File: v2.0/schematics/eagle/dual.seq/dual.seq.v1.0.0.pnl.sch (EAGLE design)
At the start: 22 parts, among them IC1 TL084P, IC2 TL084P, J1 CV3 OUT, J2 CV2 OUT, J3 CV1 OUT, J4 GATE5 OUT, J5 GATE4 OUT, J6 GATE3 OUT, J7 GATE2 OUT, J8 GATE1 OUT

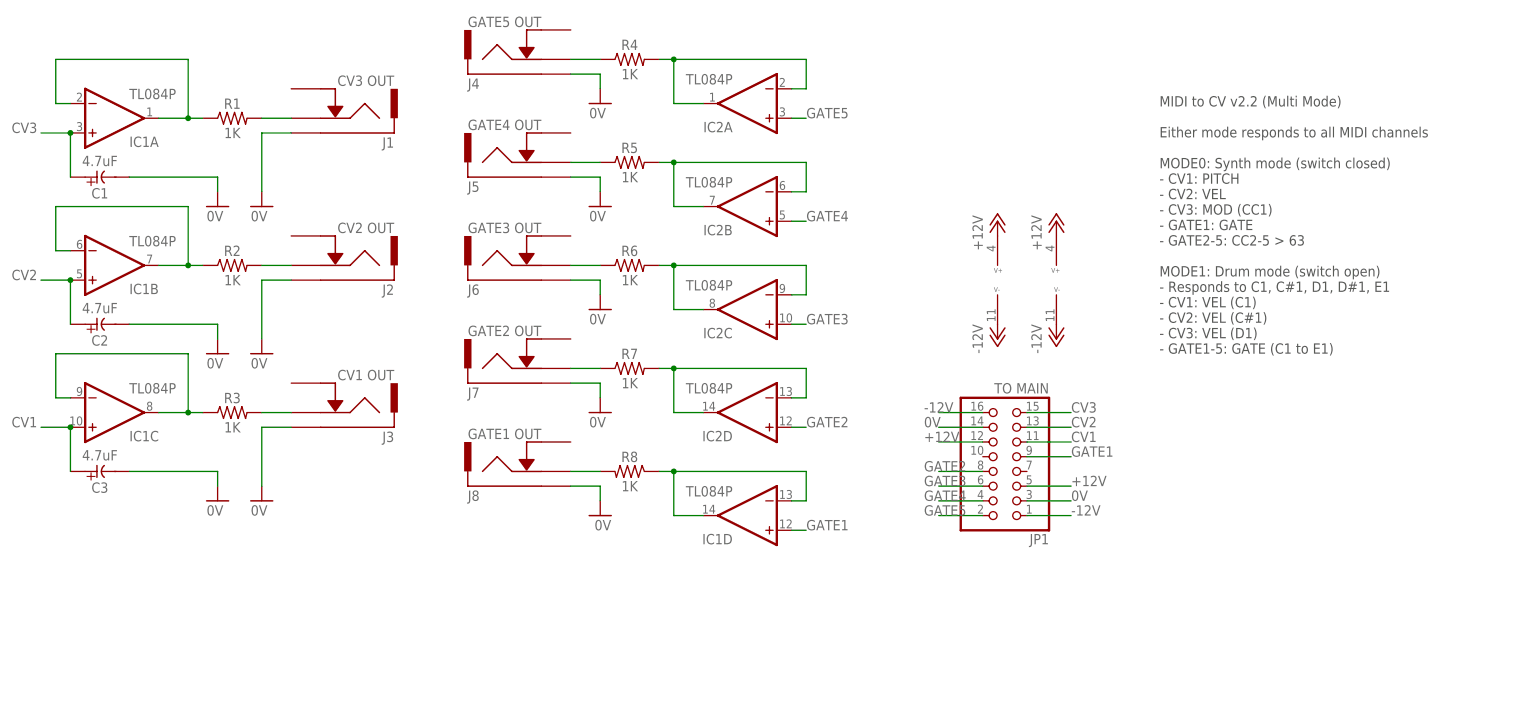
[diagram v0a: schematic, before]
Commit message: Dual seq panel schem
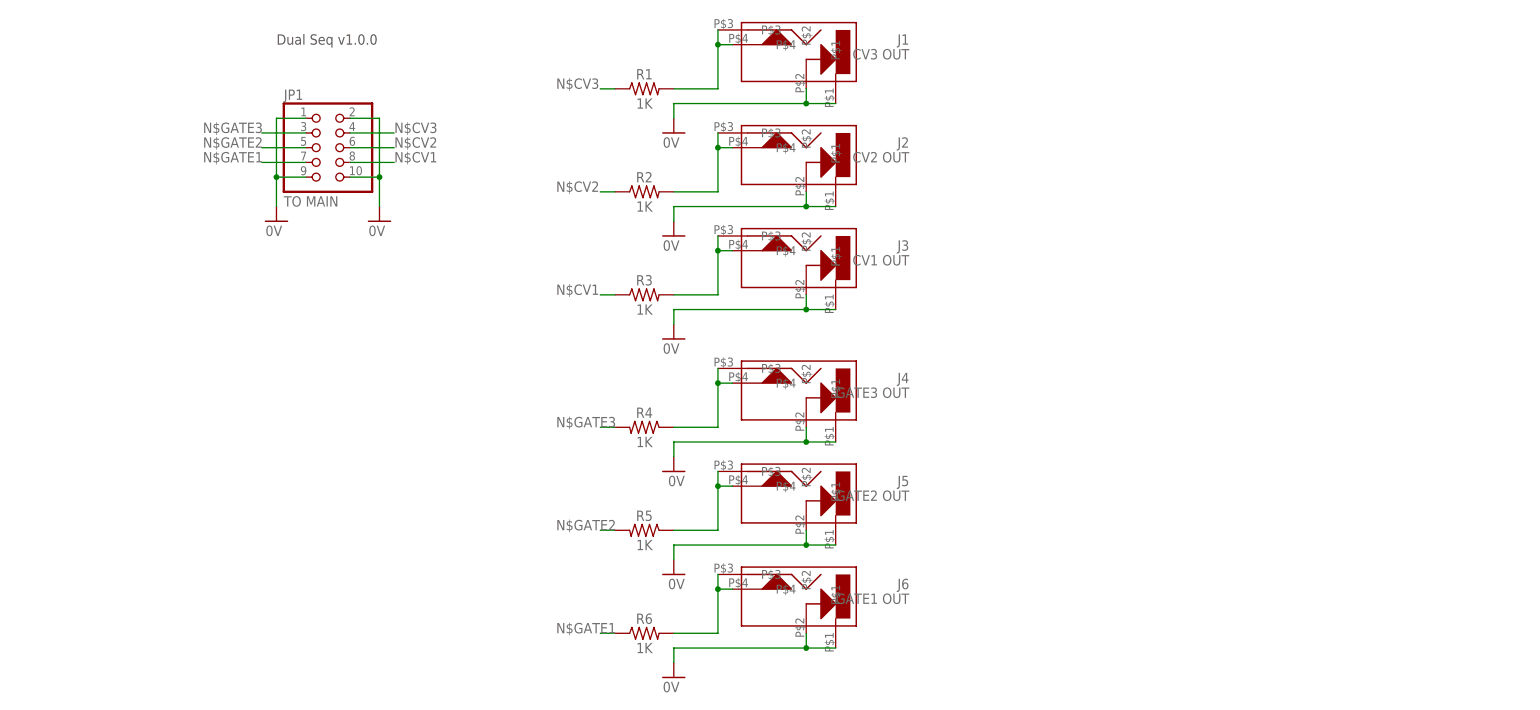
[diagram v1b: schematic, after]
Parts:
- removed C1, C2, C3: 4.7uF, _common:CE-USE2-5
- removed IC1, IC2: TL084P, _common:TL084P
- removed J7: GATE2 OUT, jacks:ACJM-MV35-2S
- removed J8: GATE1 OUT, jacks:ACJM-MV35-2S
- removed R7, R8: 1K, _common:R0309/10
- J1, J2, J3: device jacks:ACJM-MV35-2S -> jacks:CL1384
- J4: value GATE5 OUT -> GATE3 OUT; device jacks:ACJM-MV35-2S -> jacks:CL1384
- J5: value GATE4 OUT -> GATE2 OUT; device jacks:ACJM-MV35-2S -> jacks:CL1384
- J6: value GATE3 OUT -> GATE1 OUT; device jacks:ACJM-MV35-2S -> jacks:CL1384
- JP1: device pinhead:PINHD-2X8 -> pinhead:PINHD-2X5
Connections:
- removed net +12V: IC1P.V+, IC2P.V+, JP1.12, JP1.5
- removed net -12V: IC1P.V-, IC2P.V-, JP1.1, JP1.16
- removed net CV1: C3.+, IC1C.+IN, JP1.11
- removed net CV2: C2.+, IC1B.+IN, JP1.13
- removed net CV3: C1.+, IC1A.+IN, JP1.15
- removed net GATE1: IC1D.+IN, JP1.9
- removed net GATE2: IC2D.+IN, JP1.8
- removed net GATE3: IC2C.+IN, JP1.6
- removed net GATE4: IC2B.+IN, JP1.4
- removed net GATE5: IC2A.+IN, JP1.2
- removed net N$21: J4.P$2, R4.1
- removed net N$22: J5.P$2, R5.1
- removed net N$23: J6.P$2, R6.1
- removed net N$24: J7.P$2, R7.1
- removed net N$25: J8.P$2, R8.2
- removed net N$31: IC2D.-IN, IC2D.OUT, R7.2
- removed net N$35: IC2C.-IN, IC2C.OUT, R6.2
- removed net N$36: IC2B.-IN, IC2B.OUT, R5.2
- removed net N$37: IC2A.-IN, IC2A.OUT, R4.2
- removed net N$44: J1.P$2, R1.2
- removed net N$45: J2.P$2, R2.2
- removed net N$46: J3.P$2, R3.2
- removed net N$7: IC1D.-IN, IC1D.OUT, R8.1
- new net N$1: J6.P$3, J6.P$4, R6.2
- new net N$5: J2.P$3, J2.P$4, R2.2
- new net N$6: J1.P$3, J1.P$4, R1.2
- new net N$CV1: JP1.8, R3.1
- new net N$CV2: JP1.6, R2.1
- new net N$CV3: JP1.4, R1.1
- new net N$GATE1: JP1.7, R6.1
- new net N$GATE2: JP1.5, R5.2
- new net N$GATE3: JP1.3, R4.2
- net 0V: now also J1.P$2, J2.P$2, J3.P$2, J4.P$2, J5.P$2, J6.P$2, JP1.1, JP1.10, JP1.2, JP1.9; no longer C1.-, C2.-, C3.-, J7.P$1, J8.P$1, JP1.14, JP1.3
- net N$2: now also J5.P$3, J5.P$4, R5.1; no longer IC1A.-IN, IC1A.OUT, R1.1
- net N$3: now also J4.P$3, J4.P$4, R4.1; no longer IC1B.-IN, IC1B.OUT, R2.1
- net N$4: now also J3.P$3, J3.P$4, R3.2; no longer IC1C.-IN, IC1C.OUT, R3.1
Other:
- note added: "Dual Seq v1.0.0"
- note removed: "MIDI to CV v2.2 (Multi Mode) Either mode responds to all MIDI channels MODE0: Synth mode (switch closed) - CV1: PITCH - CV2: VEL - CV3: MOD (CC1) - GATE1: GATE - GATE2-5: CC2-5 > 63 MODE1: Drum mode (switch open) - Responds to C1, C#1, D1, D#1, E1 - CV1: VEL (C1) - CV2: VEL (C#1) - CV3: VEL (D1) - GATE1-5: GATE (C1 to E1)"
- moved on the sheet: R1, R2, R3, R4, R5, R6

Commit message: Added board for dual seq panel
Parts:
- R1, R2, R3, R4, R5, R6: device _common:R0309/10 -> _common:R
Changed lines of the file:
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@@
 <grid distance="0.1" unitdist="inch" unit="inch" style="lines" multiple="1" display="no" altdistance="0.01" altunitdist="inch" altunit="inch"/>
 <layers>
-<layer number="1" name="Top" color="4" fill="1" visible="no" active="no"/>
-<layer number="16" name="Bottom" color="1" fill="1" visible="no" active="no"/>
-<layer number="17" name="Pads" color="2" fill="1" visible="no" active="no"/>
-<layer number="18" name="Vias" color="2" fill="1" visible="no" active="no"/>
-<layer number="19" name="Unrouted" color="6" fill="1" visible="no" active="no"/>
-<layer number="20" name="Dimension" color="15" fill="1" visible="no" active="no"/>
-<layer number="21" name="tPlace" color="7" fill="1" visible="no" active="no"/>
-<layer number="22" name="bPlace" color="7" fill="1" visible="no" active="no"/>
-<layer number="23" name="tOrigins" color="15" fill="1" visible="no" active="no"/>
-<layer number="24" name="bOrigins" color="15" fill="1" visible="no" active="no"/>
-<layer number="25" name="tNames" color="7" fill="1" visible="no" active="no"/>
-<layer number="26" name="bNames" color="7" fill="1" visible="no" active="no"/>
-<layer number="27" name="tValues" color="7" fill="1" visible="no" active="no"/>
-<layer number="28" name="bValues" color="7" fill="1" visible="no" active="no"/>
+<layer number="1" name="Top" color="4" fill="1" visible="yes" active="no"/>
+<layer number="16" name="Bottom" color="1" fill="1" visible="yes" active="no"/>
+<layer number="17" name="Pads" color="2" fill="1" visible="yes" active="no"/>
+<layer number="18" name="Vias" color="2" fill="1" visible="yes" active="no"/>
+<layer number="19" name="Unrouted" color="6" fill="1" visible="yes" active="no"/>
+<layer number="20" name="Dimension" color="15" fill="1" visible="yes" active="no"/>
+<layer number="21" name="tPlace" color="7" fill="1" visible="yes" active="no"/>
+<layer number="22" name="bPlace" color="7" fill="1" visible="yes" active="no"/>
+<layer number="23" name="tOrigins" color="15" fill="1" visible="yes" active="no"/>
+<layer number="24" name="bOrigins" color="15" fill="1" visible="yes" active="no"/>
+<layer number="25" name="tNames" color="7" fill="1" visible="yes" active="no"/>
+<layer number="26" name="bNames" color="7" fill="1" visible="yes" active="no"/>
+<layer number="27" name="tValues" color="7" fill="1" visible="yes" active="no"/>
+<layer number="28" name="bValues" color="7" fill="1" visible="yes" active="no"/>
 <layer number="29" name="tStop" color="7" fill="3" visible="no" active="no"/>
 <layer number="30" name="bStop" color="7" fill="6" visible="no" active="no"/>
@@
 <layer number="35" name="tGlue" color="7" fill="4" visible="no" active="no"/>
 <layer number="36" name="bGlue" color="7" fill="5" visible="no" active="no"/>
-<layer number="37" name="tTest" color="7" fill="1" visible="no" active="no"/>
-<layer number="38" name="bTest" color="7" fill="1" visible="no" active="no"/>
+<layer number="37" name="tTest" color="7" fill="1" visible="yes" active="no"/>
+<layer number="38" name="bTest" color="7" fill="1" visible="yes" active="no"/>
 <layer number="39" name="tKeepout" color="4" fill="11" visible="no" active="no"/>
 <layer number="40" name="bKeepout" color="1" fill="11" visible="no" active="no"/>
@@
 <layer number="44" name="Drills" color="7" fill="1" visible="no" active="no"/>
 <layer number="45" name="Holes" color="7" fill="1" visible="no" active="no"/>
-<layer number="46" name="Milling" color="3" fill="1" visible="no" active="no"/>
-<layer number="47" name="Measures" color="7" fill="1" visible="no" active="no"/>
-<layer number="48" name="Document" color="7" fill="1" visible="no" active="no"/>
-<layer number="49" name="Reference" color="7" fill="1" visible="no" active="no"/>
-<layer number="50" name="dxf" color="7" fill="1" visible="no" active="no"/>
-<layer number="51" name="tDocu" color="7" fill="1" visible="no" active="no"/>
-<layer number="52" name="bDocu" color="7" fill="1" visible="no" active="no"/>
+<layer number="46" name="Milling" color="3" fill="1" visible="yes" active="no"/>
+<layer number="47" name="Measures" color="7" fill="1" visible="yes" active="no"/>
+<layer number="48" name="Document" color="7" fill="1" visible="yes" active="no"/>
+<layer number="49" name="Reference" color="7" fill="1" visible="yes" active="no"/>
+<layer number="50" name="dxf" color="7" fill="1" visible="yes" active="no"/>
+<layer number="51" name="tDocu" color="7" fill="1" visible="yes" active="no"/>
+<layer number="52" name="bDocu" color="7" fill="1" visible="yes" active="no"/>
 <layer number="90" name="Modules" color="5" fill="1" visible="yes" active="yes"/>
 <layer number="91" name="Nets" color="2" fill="1" visible="yes" active="yes"/>
@@
 <layer number="97" name="Info" color="7" fill="1" visible="yes" active="yes"/>
 <layer number="98" name="Guide" color="6" fill="1" visible="yes" active="yes"/>
+<layer number="99" name="SpiceOrder" color="5" fill="1" visible="yes" active="yes"/>
 <layer number="100" name="Caption" color="15" fill="0" visible="yes" active="yes"/>
 <layer number="101" name="Patch_Top" color="7" fill="1" visible="yes" active="yes"/>
@@
 <part name="GND6" library="supply1" deviceset="0V" device=""/>
 <part name="GND7" library="supply1" deviceset="0V" device=""/>
-<part name="R1" library="_common" deviceset="R" device="0309/10" value="1K"/>
-<part name="R2" library="_common" deviceset="R" device="0309/10" value="1K"/>
-<part name="R3" library="_common" deviceset="R" device="0309/10" value="1K"/>
-<part name="R6" library="_common" deviceset="R" device="0309/10" value="1K"/>
-<part name="R4" library="_common" deviceset="R" device="0309/10" value="1K"/>
-<part name="R5" library="_common" deviceset="R" device="0309/10" value="1K"/>
+<part name="R1" library="_common" deviceset="R" device="" value="1K"/>
+<part name="R2" library="_common" deviceset="R" device="" value="1K"/>
+<part name="R3" library="_common" deviceset="R" device="" value="1K"/>
+<part name="R6" library="_common" deviceset="R" device="" value="1K"/>
+<part name="R4" library="_common" deviceset="R" device="" value="1K"/>
+<part name="R5" library="_common" deviceset="R" device="" value="1K"/>
 <part name="J4" library="jacks" deviceset="CL1384" device="" value="GATE3 OUT"/>
 <part name="J5" library="jacks" deviceset="CL1384" device="" value="GATE2 OUT"/>

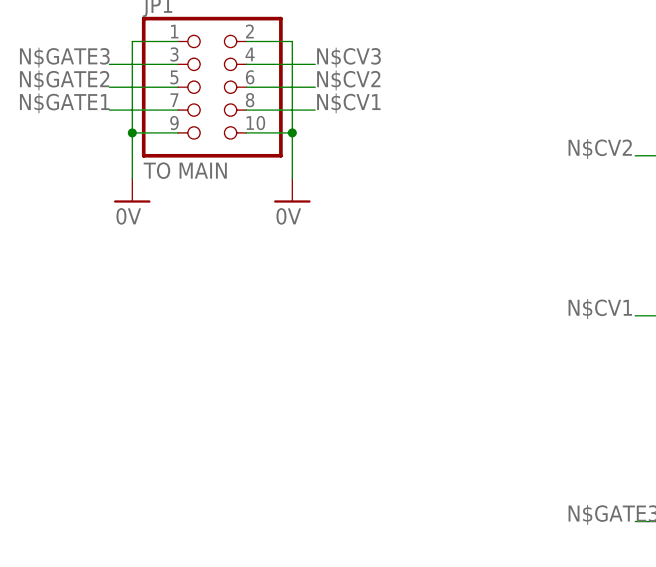
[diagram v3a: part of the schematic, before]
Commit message: Added note on inverted header to dual.seq pnl
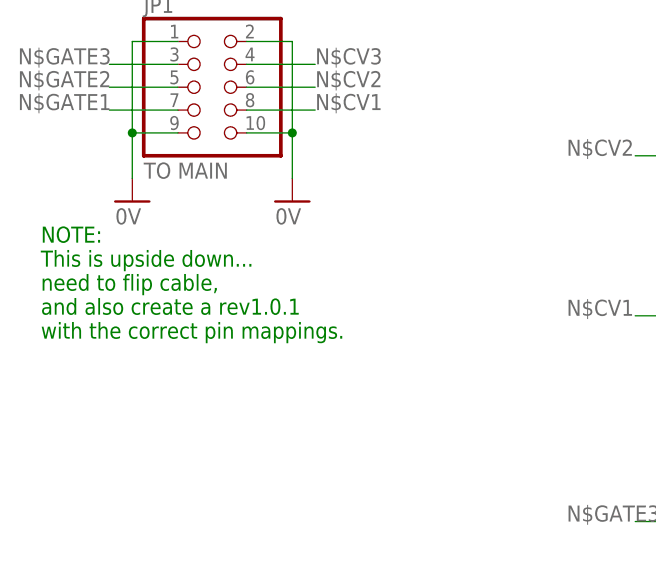
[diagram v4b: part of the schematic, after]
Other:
- note added: "NOTE: This is upside down... need to flip cable, and also create a rev1.0.1 with the correct pin mappings."
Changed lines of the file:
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@@
 <?xml version="1.0" encoding="utf-8"?>
 <!DOCTYPE eagle SYSTEM "eagle.dtd">
-<eagle version="7.7.0">
+<eagle version="7.2.0">
 <drawing>
 <settings>
@@
 <text x="-10.16" y="119.38" size="1.778" layer="97">Dual Seq v1.0.0</text>
 <frame x1="-38.1" y1="0" x2="111.76" y2="134.62" columns="8" rows="5" layer="91"/>
+<text x="-20.32" y="73.66" size="1.778" layer="91">NOTE:
+This is upside down...
+need to flip cable,
+and also create a rev1.0.1
+with the correct pin mappings.</text>
 </plain>
 <instances>
@@
 </schematic>
 </drawing>
+<compatibility>
+<note version="6.3" minversion="6.2.2" severity="warning">
+Since Version 6.2.2 text objects can contain more than one line,
+which will not be processed correctly with this version.
+</note>
+</compatibility>
 </eagle>
